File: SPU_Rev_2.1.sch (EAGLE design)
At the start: 258 parts, among them Q1 12MHz

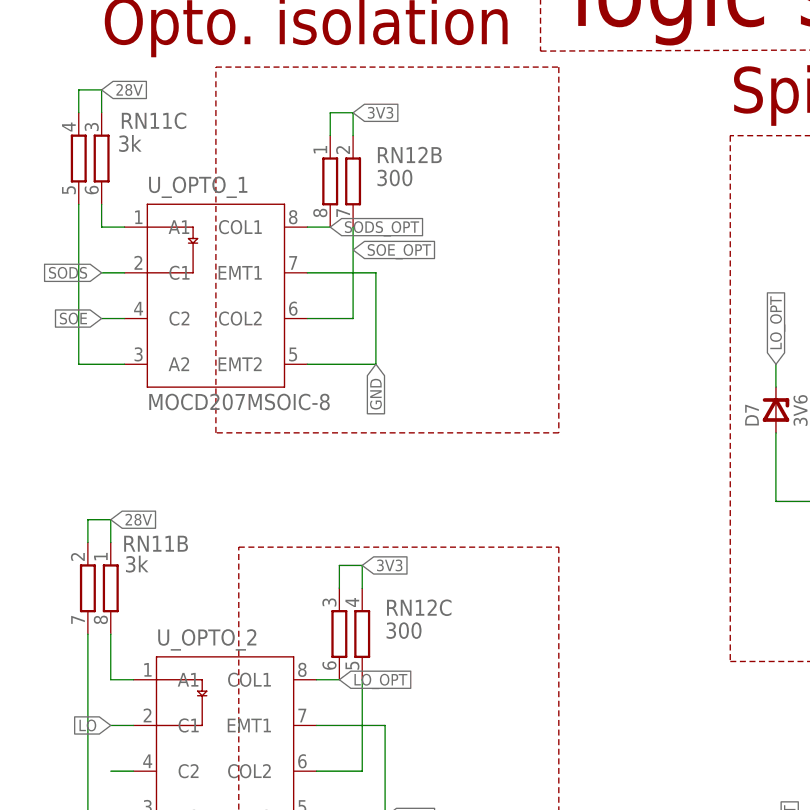
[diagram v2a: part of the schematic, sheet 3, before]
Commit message: Opto Pull-up adjusted
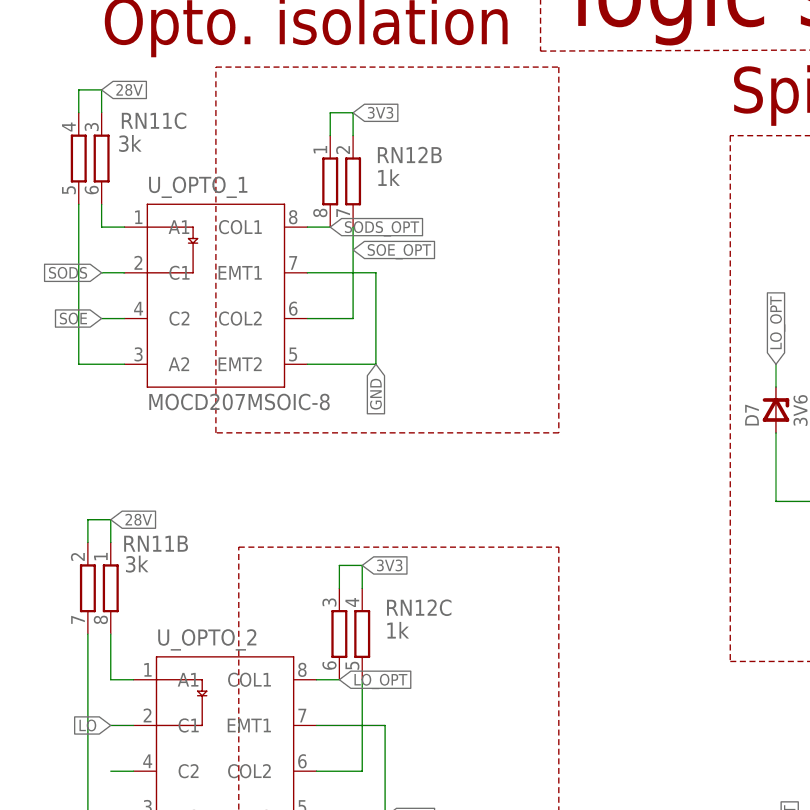
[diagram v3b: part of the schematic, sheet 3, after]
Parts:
- C77, C78: value (none) -> 100n
- RN12: value 300 -> 1k
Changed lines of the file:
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@@
 <part name="RN11" library="resistor-dil" library_urn="urn:adsk.eagle:library:342" deviceset="4R-N" device="EXBS8V" package3d_urn="urn:adsk.eagle:package:24925/1" value="3k"/>
 <part name="U_OPTO_2" library="Opto-Electronic" library_urn="urn:adsk.eagle:library:16378487" deviceset="MOCD207M" device="SOIC-8" package3d_urn="urn:adsk.eagle:package:16378512/1"/>
-<part name="RN12" library="resistor-dil" library_urn="urn:adsk.eagle:library:342" deviceset="4R-N" device="EXBS8V" package3d_urn="urn:adsk.eagle:package:24925/1" value="300"/>
+<part name="RN12" library="resistor-dil" library_urn="urn:adsk.eagle:library:342" deviceset="4R-N" device="EXBS8V" package3d_urn="urn:adsk.eagle:package:24925/1" value="1k"/>
 <part name="U_MAX488" library="maxim" library_urn="urn:adsk.eagle:library:269" deviceset="MAX488" device="CSA" package3d_urn="urn:adsk.eagle:package:17511/1"/>
 <part name="R10" library="rcl" deviceset="R-EU_" device="R0805" value="500"/>
@@
 <part name="C76" library="aSparkFun" deviceset="CAP" device="0603-CAP" value="100n"/>
 <part name="U$8" library="everlight-fiber-optics-spdif" deviceset="PLT131" device="PLT131-T1" value="PLT131PLT131-T1"/>
-<part name="C77" library="rcl" library_urn="urn:adsk.eagle:library:334" deviceset="C-EU" device="C1206" package3d_urn="urn:adsk.eagle:package:23618/2"/>
+<part name="C77" library="rcl" library_urn="urn:adsk.eagle:library:334" deviceset="C-EU" device="C1206" package3d_urn="urn:adsk.eagle:package:23618/2" value="100n"/>
 <part name="U$9" library="everlight-fiber-optics-spdif" deviceset="PLR135" device=""/>
-<part name="C78" library="rcl" library_urn="urn:adsk.eagle:library:334" deviceset="C-EU" device="C1206" package3d_urn="urn:adsk.eagle:package:23618/2"/>
+<part name="C78" library="rcl" library_urn="urn:adsk.eagle:library:334" deviceset="C-EU" device="C1206" package3d_urn="urn:adsk.eagle:package:23618/2" value="100n"/>
 </parts>
 <sheets>
@@
 <wire x1="273.05" y1="154.94" x2="200.66" y2="154.94" width="0.4572" layer="88"/>
 <wire x1="200.66" y1="154.94" x2="200.66" y2="212.09" width="0.4572" layer="88"/>
+<wire x1="123.19" y1="195.58" x2="182.88" y2="195.58" width="0.4572" layer="88"/>
+<wire x1="182.88" y1="195.58" x2="182.88" y2="288.29" width="0.4572" layer="88"/>
+<wire x1="182.88" y1="288.29" x2="123.19" y2="288.29" width="0.4572" layer="88"/>
+<wire x1="123.19" y1="288.29" x2="123.19" y2="195.58" width="0.4572" layer="88"/>
+<wire x1="405.13" y1="-280.67" x2="438.15" y2="-280.67" width="0.4572" layer="88"/>
+<wire x1="438.15" y1="-280.67" x2="438.15" y2="-322.58" width="0.4572" layer="88"/>
+<wire x1="438.15" y1="-322.58" x2="405.13" y2="-322.58" width="0.4572" layer="88"/>
+<wire x1="405.13" y1="-322.58" x2="405.13" y2="-280.67" width="0.4572" layer="88"/>
 </plain>
 <instances>

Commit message: Minor adjustments
adjusted zener values, added optinal trimresistors for voltage setting.
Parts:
- added R64, R65: inf, rcl:R-EU_R0805
- added R66: inf, rcl:R-TRIMM3224X
- D1, D2, D5, D6: value 6V -> 5V6
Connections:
- new net N$17: R64.2, R65.2, R66.S, U_TRACODCDC.TRIM
- net 5V: now also R65.1, R66.E
- net GND: now also R64.1, R66.A
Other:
- note added: "TODO: input fuse?"
- note added: "Trim: up: R=(12775/U_out) - 2050 down: R=((U_out * 5110) / (5 - U_out)) - 2050"
- note added: "no testing needed"
- note removed: "TODO for Rev 2.1 12 DMS-Paare (ergo 24 DMS), pro SPU 6 DMS-Paare 3 PT100 2 DMS pro ADC https://www.hbm.com/de/7163/die-wheatstonesche-brueckenschaltung-kurz-erklaert/ -> 3. Poisson H-Brücke"
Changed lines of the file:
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@@
 <part name="C2" library="rcl" deviceset="C-EU" device="C0603" value="22p"/>
 <part name="U_LT1528" library="aSparkFun" deviceset="LT1528" device=""/>
-<part name="D1" library="diodes" deviceset="DZ" device="MELF" value="6V"/>
-<part name="D2" library="diodes" deviceset="DZ" device="MELF" value="6V"/>
+<part name="D1" library="diodes" deviceset="DZ" device="MELF" value="5V6"/>
+<part name="D2" library="diodes" deviceset="DZ" device="MELF" value="5V6"/>
 <part name="D3" library="diodes" deviceset="DZ" device="MELF" value="3V6"/>
 <part name="D4" library="diodes" deviceset="DZ" device="MELF" value="3V6"/>
@@
 <part name="U_MAX488" library="maxim" library_urn="urn:adsk.eagle:library:269" deviceset="MAX488" device="CSA" package3d_urn="urn:adsk.eagle:package:17511/1"/>
 <part name="R10" library="rcl" deviceset="R-EU_" device="R0805" value="500"/>
-<part name="D5" library="diodes" deviceset="DZ" device="MELF" value="6V"/>
-<part name="D6" library="diodes" deviceset="DZ" device="MELF" value="6V"/>
+<part name="D5" library="diodes" deviceset="DZ" device="MELF" value="5V6"/>
+<part name="D6" library="diodes" deviceset="DZ" device="MELF" value="5V6"/>
 <part name="D7" library="diodes" deviceset="DZ" device="MELF" value="3V6"/>
 <part name="D8" library="diodes" deviceset="DZ" device="MELF" value="3V6"/>
@@
 <part name="U$9" library="everlight-fiber-optics-spdif" deviceset="PLR135" device=""/>
 <part name="C78" library="rcl" library_urn="urn:adsk.eagle:library:334" deviceset="C-EU" device="C1206" package3d_urn="urn:adsk.eagle:package:23618/2" value="100n"/>
+<part name="R64" library="rcl" library_urn="urn:adsk.eagle:library:334" deviceset="R-EU_" device="R0805" package3d_urn="urn:adsk.eagle:package:23553/2" value="inf"/>
+<part name="R65" library="rcl" library_urn="urn:adsk.eagle:library:334" deviceset="R-EU_" device="R0805" package3d_urn="urn:adsk.eagle:package:23553/2" value="inf"/>
+<part name="R66" library="rcl" library_urn="urn:adsk.eagle:library:334" deviceset="R-TRIMM" device="3224X" package3d_urn="urn:adsk.eagle:package:23732/1" value="inf"/>
 </parts>
 <sheets>
@@
   UART</text>
 <text x="227.076" y="128.524" size="5.08" layer="94">FLASH  mem</text>
-<text x="45.72" y="226.06" size="5.08" layer="94">V. Reg</text>
+<text x="12.7" y="220.98" size="5.08" layer="94">V. Reg</text>
 <wire x1="133.35" y1="269.24" x2="138.43" y2="269.24" width="0.1524" layer="94"/>
 <wire x1="138.43" y1="269.24" x2="138.43" y2="267.97" width="0.1524" layer="94"/>
@@
 <wire x1="7.62" y1="287.02" x2="7.62" y2="236.22" width="0.1524" layer="94" style="shortdash"/>
 <wire x1="7.62" y1="236.22" x2="104.14" y2="236.22" width="0.1524" layer="94" style="shortdash"/>
-<wire x1="60.96" y1="223.52" x2="60.96" y2="190.5" width="0.1524" layer="94" style="shortdash"/>
-<wire x1="60.96" y1="190.5" x2="116.84" y2="190.5" width="0.1524" layer="94" style="shortdash"/>
-<wire x1="60.96" y1="223.52" x2="116.84" y2="223.52" width="0.1524" layer="94" style="shortdash"/>
-<wire x1="116.84" y1="223.52" x2="116.84" y2="190.5" width="0.1524" layer="94" style="shortdash"/>
+<wire x1="60.96" y1="227.33" x2="60.96" y2="184.15" width="0.1524" layer="94" style="shortdash"/>
+<wire x1="60.96" y1="184.15" x2="116.84" y2="184.15" width="0.1524" layer="94" style="shortdash"/>
+<wire x1="60.96" y1="227.33" x2="116.84" y2="227.33" width="0.1524" layer="94" style="shortdash"/>
+<wire x1="116.84" y1="227.33" x2="116.84" y2="184.15" width="0.1524" layer="94" style="shortdash"/>
 <wire x1="96.52" y1="180.34" x2="96.52" y2="148.59" width="0.1524" layer="94" style="shortdash"/>
 <wire x1="96.52" y1="148.59" x2="25.4" y2="148.59" width="0.1524" layer="94" style="shortdash"/>
@@
 <wire x1="25.4" y1="180.34" x2="96.52" y2="180.34" width="0.1524" layer="94" style="shortdash"/>
 <text x="200.66" y="-99.568" size="7.62" layer="94">all logic sided on this page</text>
-<text x="523.24" y="254" size="5.08" layer="94">TODO for Rev 2.1
-   12 DMS-Paare (ergo 24 DMS), pro SPU 6 DMS-Paare
-   3 PT100
-   2 DMS pro ADC
-https://www.hbm.com/de/7163/die-wheatstonesche-brueckenschaltung-kurz-erklaert/ -&gt; 3. Poisson H-Brücke</text>
+<text x="389.89" y="241.3" size="5.08" layer="94">TODO:
+input fuse?</text>
 <text x="322.58" y="-137.16" size="1.27" layer="97">3dB attenuation @ 1989Hz</text>
 <text x="294.64" y="-160.02" size="1.27" layer="97">WE-SL3 SMT COMMON
@@
 <wire x1="182.88" y1="288.29" x2="123.19" y2="288.29" width="0.4572" layer="88"/>
 <wire x1="123.19" y1="288.29" x2="123.19" y2="195.58" width="0.4572" layer="88"/>
-<wire x1="405.13" y1="-280.67" x2="438.15" y2="-280.67" width="0.4572" layer="88"/>
-<wire x1="438.15" y1="-280.67" x2="438.15" y2="-322.58" width="0.4572" layer="88"/>
-<wire x1="438.15" y1="-322.58" x2="405.13" y2="-322.58" width="0.4572" layer="88"/>
-<wire x1="405.13" y1="-322.58" x2="405.13" y2="-280.67" width="0.4572" layer="88"/>
+<wire x1="394.97" y1="-278.13" x2="445.77" y2="-278.13" width="0.4572" layer="88"/>
+<wire x1="445.77" y1="-278.13" x2="445.77" y2="-326.39" width="0.4572" layer="88"/>
+<wire x1="445.77" y1="-326.39" x2="394.97" y2="-326.39" width="0.4572" layer="88"/>
+<wire x1="394.97" y1="-326.39" x2="394.97" y2="-278.13" width="0.4572" layer="88"/>
+<wire x1="6.35" y1="288.29" x2="105.41" y2="288.29" width="0.4572" layer="88"/>
+<wire x1="105.41" y1="288.29" x2="105.41" y2="234.95" width="0.4572" layer="88"/>
+<wire x1="105.41" y1="234.95" x2="6.35" y2="234.95" width="0.4572" layer="88"/>
+<wire x1="6.35" y1="234.95" x2="6.35" y2="288.29" width="0.4572" layer="88"/>
+<wire x1="382.27" y1="275.59" x2="466.09" y2="275.59" width="0.4572" layer="88" style="shortdash"/>
+<wire x1="466.09" y1="275.59" x2="466.09" y2="285.75" width="0.4572" layer="88" style="shortdash"/>
+<wire x1="466.09" y1="285.75" x2="382.27" y2="285.75" width="0.4572" layer="88" style="shortdash"/>
+<wire x1="382.27" y1="285.75" x2="382.27" y2="275.59" width="0.4572" layer="88" style="shortdash"/>
+<text x="387.35" y="278.13" size="5.08" layer="88">no testing needed</text>
+<wire x1="285.75" y1="280.67" x2="318.77" y2="280.67" width="0.4572" layer="88" style="shortdash"/>
+<wire x1="318.77" y1="280.67" x2="318.77" y2="166.37" width="0.4572" layer="88" style="shortdash"/>
+<wire x1="318.77" y1="166.37" x2="285.75" y2="166.37" width="0.4572" layer="88" style="shortdash"/>
+<wire x1="285.75" y1="166.37" x2="285.75" y2="280.67" width="0.4572" layer="88" style="shortdash"/>
+<wire x1="196.85" y1="280.67" x2="196.85" y2="219.71" width="0.4572" layer="88" style="shortdash"/>
+<wire x1="196.85" y1="219.71" x2="255.27" y2="219.71" width="0.4572" layer="88" style="shortdash"/>
+<wire x1="255.27" y1="219.71" x2="255.27" y2="280.67" width="0.4572" layer="88" style="shortdash"/>
+<wire x1="255.27" y1="280.67" x2="196.85" y2="280.67" width="0.4572" layer="88" style="shortdash"/>
+<text x="81.28" y="217.17" size="1.27" layer="94">Trim:
+  up:
+    R=(12775/U_out) - 2050
+  down:
+    R=((U_out * 5110) / (5 - U_out)) - 2050</text>
 </plain>
 <instances>
@@
 <attribute name="VALUE" x="77.724" y="267.335" size="1.778" layer="96"/>
 </instance>
+<instance part="R64" gate="G$1" x="86.36" y="198.12" smashed="yes" rot="R180">
+<attribute name="NAME" x="90.17" y="196.6214" size="1.778" layer="95" rot="R180"/>
+<attribute name="VALUE" x="90.17" y="201.422" size="1.778" layer="96" rot="R180"/>
+</instance>
+<instance part="R65" gate="G$1" x="86.36" y="187.96" smashed="yes" rot="R180">
+<attribute name="NAME" x="90.17" y="186.4614" size="1.778" layer="95" rot="R180"/>
+<attribute name="VALUE" x="90.17" y="191.262" size="1.778" layer="96" rot="R180"/>
+</instance>
+<instance part="R66" gate="G$1" x="92.71" y="193.04" smashed="yes" rot="R180">
+<attribute name="NAME" x="96.52" y="192.659" size="1.778" layer="95"/>
+<attribute name="VALUE" x="96.52" y="190.5" size="1.778" layer="96"/>
+</instance>
 </instances>
 <busses>
@@
 <junction x="68.58" y="274.32"/>
 </segment>
+<segment>
+<pinref part="R64" gate="G$1" pin="1"/>
+<wire x1="91.44" y1="198.12" x2="92.71" y2="198.12" width="0.1524" layer="91"/>
+<label x="92.71" y="198.12" size="1.27" layer="95" xref="yes"/>
+<pinref part="R66" gate="G$1" pin="A"/>
+</segment>
 </net>
 <net name="3V3" class="0">
@@
 <junction x="25.4" y="264.16"/>
 </segment>
+<segment>
+<pinref part="R65" gate="G$1" pin="1"/>
+<pinref part="R66" gate="G$1" pin="E"/>
+<wire x1="91.44" y1="187.96" x2="92.71" y2="187.96" width="0.1524" layer="91"/>
+<label x="92.71" y="187.96" size="1.27" layer="95" xref="yes"/>
+</segment>
 </net>
 <net name="28V" class="0">
@@
 </segment>
 </net>
+<net name="N$17" class="0">
+<segment>
+<pinref part="R64" gate="G$1" pin="2"/>
+<pinref part="U_TRACODCDC" gate="G$1" pin="TRIM"/>
+<wire x1="81.28" y1="198.12" x2="78.74" y2="198.12" width="0.1524" layer="91"/>
+<pinref part="R65" gate="G$1" pin="2"/>
+<wire x1="78.74" y1="198.12" x2="76.2" y2="198.12" width="0.1524" layer="91"/>
+<wire x1="81.28" y1="187.96" x2="78.74" y2="187.96" width="0.1524" layer="91"/>
+<wire x1="78.74" y1="187.96" x2="78.74" y2="193.04" width="0.1524" layer="91"/>
+<junction x="78.74" y="198.12"/>
+<pinref part="R66" gate="G$1" pin="S"/>
+<wire x1="78.74" y1="193.04" x2="78.74" y2="198.12" width="0.1524" layer="91"/>
+<wire x1="87.63" y1="193.04" x2="78.74" y2="193.04" width="0.1524" layer="91"/>
+<junction x="78.74" y="193.04"/>
+</segment>
+</net>
